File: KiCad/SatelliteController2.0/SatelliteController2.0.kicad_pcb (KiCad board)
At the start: 2 copper layers, 150 x 100 mm, 222 parts, among them J1 CONN_ICSP, J10 CONN_ISOLATED_RS485_REPEATER, J11 CONN_UMBILICAL, J12 CONN_ISOLATED_RS485_REPEATER, J13 CONN_ISOLATED_RS485, J14 RELAY_POWER, J15 IGNITOR, J16 CONN_SORENOID_VALVE, J2 CONN_USB, J3 USB_C_Receptacle_USB2.0_16P, J4 TO_CONVERTER, J5 FROM_CONVERTER, J6 DC_IN, J7 CONN_STATUS_PANEL, J8 CONN_PANEL_BOARD_2, J9 CONN_N2O_PRESS, Q1 TJ8S06M3L, Q10 AO3400A, Q11 AO3400A, Q12 AO3400A, Q13 AO3400A, Q2 2SC3325-Y, Q3 TJ8S06M3L, Q4 AO3400A, Q5 AO3400A, Q6 AO3400A, Q7 AO3400A, Q8 AO3400A, Q9 AO3400A, SW1 RUN_SW, SW2 KILL_SW, SW3 SAFETY_SW, SW4 RESET_SW, SW5 CHECK_SW, U1 ATMEGA2560-16AUR, U10 TLP785F, U11 TLP785F, U12 MCP3208, U2 FT232RNL, U3 USBLC6-2SC6, U4 TPS2116DRL, U5 NJM7805SDL1, U6 INA219BIDCNT, U7 INA219BIDCNT, U8 ADS1115IDGS, U9 ADM2587E, Y1 HUSG-16.000-20

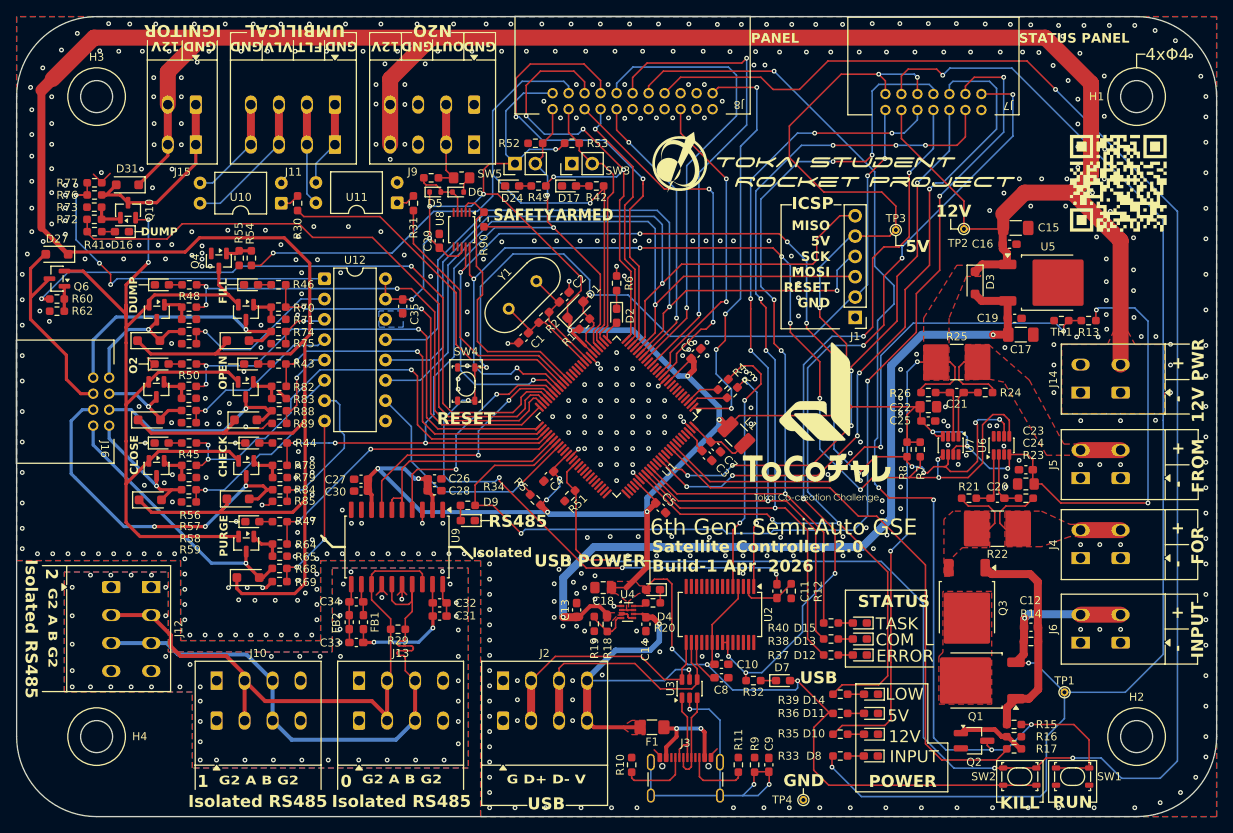
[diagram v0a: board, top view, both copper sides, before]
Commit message: シルクなどを調整
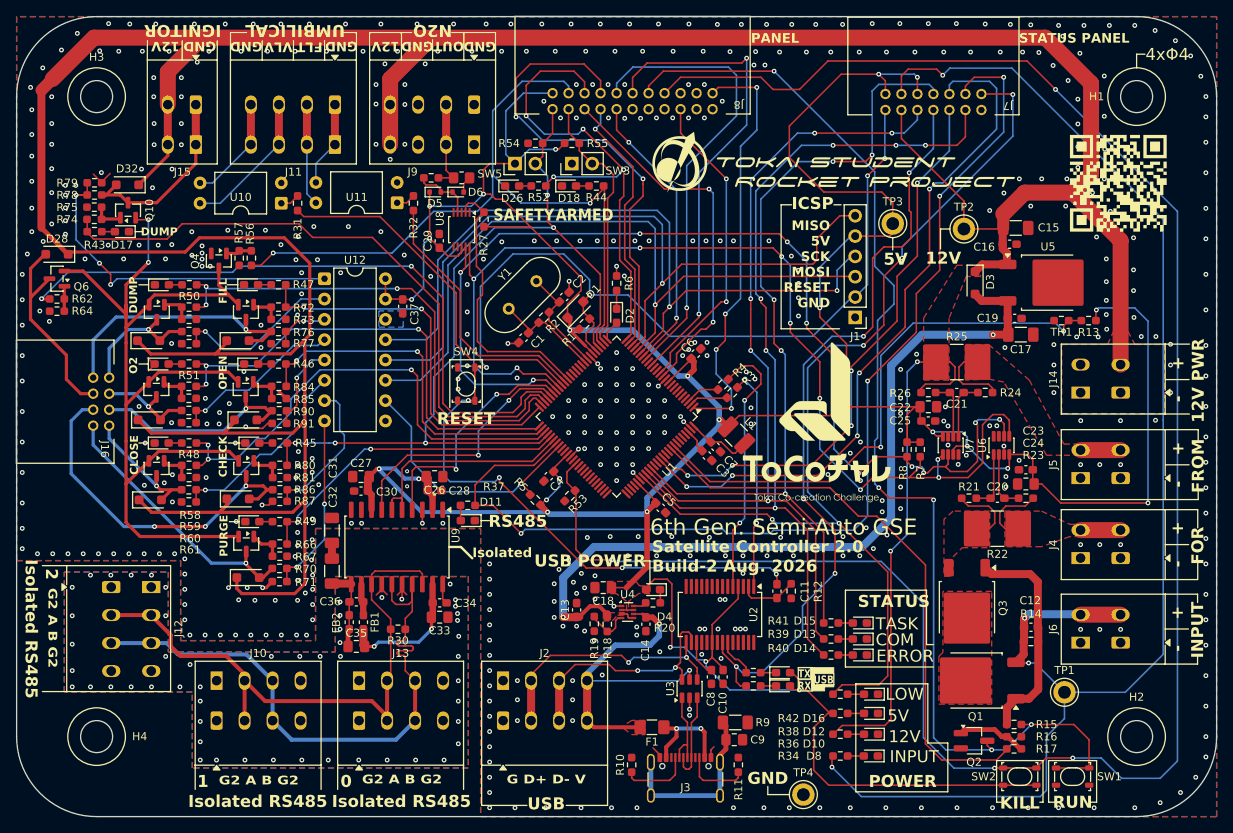
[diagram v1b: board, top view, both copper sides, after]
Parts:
- added C31: 470pF, Capacitor_SMD:C_1206_3216Metric_Pad1.33x1.80mm_HandSolder, F.Cu at (112.7, 119.4)
- added C32: 470pF, Capacitor_SMD:C_1206_3216Metric_Pad1.33x1.80mm_HandSolder, F.Cu at (112.7, 124.5)
- added D9: LED_O, LED_SMD:LED_0603_1608Metric_Pad1.05x0.95mm_HandSolder, F.Cu at (169.1, 137.2)
- added R35: 1kR, Resistor_SMD:R_0603_1608Metric_Pad0.98x0.95mm_HandSolder, F.Cu at (165.4, 137.2)
- C20, C21: value uF -> 0.1uF
- C26, C27: value 0.1uF -> 10uF; footprint Capacitor_SMD:C_0603_1608Metric_Pad1.08x0.95mm_HandSolder -> Capacitor_SMD:C_0805_2012Metric_Pad1.18x1.45mm_HandSolder
- C28, C30: value 0.01uF -> 0.1uF
- C33: renamed from C31; value 0.1uF -> 10uF; footprint Capacitor_SMD:C_0603_1608Metric_Pad1.08x0.95mm_HandSolder -> Capacitor_SMD:C_0805_2012Metric_Pad1.18x1.45mm_HandSolder
- C34: renamed from C32; value 0.01uF -> 0.1uF
- C35: renamed from C33; value 0.1uF -> 10uF; footprint Capacitor_SMD:C_0603_1608Metric_Pad1.08x0.95mm_HandSolder -> Capacitor_SMD:C_0805_2012Metric_Pad1.18x1.45mm_HandSolder
- C36: renamed from C34; value 0.01uF -> 0.1uF
- C9: value 4.7uF -> 10nF; footprint Capacitor_SMD:C_0603_1608Metric_Pad1.08x0.95mm_HandSolder -> Capacitor_SMD:C_0805_2012Metric_Pad1.18x1.45mm_HandSolder
- D2: value LED_G -> LED_O
- D7: value LED_B -> LED_G
- R18: value 348kR ±1% -> 348kR 1%
- R19: value 100kR ±1% -> 100kR 1%
- R21, R23, R24, R26: value 0R -> 10R
- R9: footprint Resistor_SMD:R_0603_1608Metric_Pad0.98x0.95mm_HandSolder -> Resistor_SMD:R_1206_3216Metric_Pad1.30x1.75mm_HandSolder
- TP1, TP2, TP3, TP4: footprint TestPoint:TestPoint_THTPad_D1.0mm_Drill0.5mm -> TestPoint:TestPoint_Keystone_5005-5009_Compact
- moved R9 5.82 mm to (163.1, 143.4), turned to 0 degrees
- moved C9 5.34 mm to (163.0, 145.5), turned to 180 degrees
- moved C10 1.60 mm to (161.6, 137.7), turned to 90 degrees
- moved C8 1.26 mm to (160.1, 137.7), turned to 90 degrees
- moved TP3 0.89 mm to (182.8, 81.0)
- moved TP4 0.67 mm to (171.6, 152.4)
- moved D7 0.66 mm to (169.1, 138.8)
- moved R33 0.66 mm to (165.4, 138.8)
- moved C35 0.50 mm to (115.7, 133.9)
- moved C27 0.33 mm to (116.3, 112.7)
- moved C26 0.29 mm to (125.5, 112.7)
- moved C33 0.14 mm to (126.1, 130.2)
- renumbered C35 to C37, D9 to D11, D11 to D12, D12 to D14, D14 to D16, D16 to D17, D17 to D18, D18 to D20, D20 to D22, D22 to D23, D23 to D24, D24 to D26, D26 to D27, D27 to D28, D28 to D29, D29 to D30, D30 to D31, D31 to D32, D32 to D33, D33 to D34, D34 to D35, R90 to R27, R27 to R28, R28 to R29, R29 to R30, R30 to R31, R31 to R32, R32 to R33, R33 to R34, R35 to R36, R34 to R37, R36 to R38, R38 to R39, R37 to R40, R40 to R41, R39 to R42, R41 to R43, R42 to R44, R44 to R45, R43 to R46, R46 to R47, R45 to R48, R47 to R49, R48 to R50, R50 to R51, R49 to R52, R51 to R53, R52 to R54, R53 to R55, R54 to R56, R55 to R57, R56 to R58, R57 to R59, R58 to R60, R59 to R61, R60 to R62, R61 to R63, R62 to R64, R63 to R65, R64 to R66, R65 to R67, R66 to R68, R67 to R69, R68 to R70, R69 to R71, R70 to R72, R71 to R73, R72 to R74, R73 to R75, R74 to R76, R75 to R77, R76 to R78, R77 to R79, R78 to R80, R79 to R81, R80 to R82, R81 to R83, R82 to R84, R83 to R85, R84 to R86, R85 to R87, R86 to R88, R87 to R89, R88 to R90, R89 to R91
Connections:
- U2 pad 23: CONN_LED_USB_ACCESS -> LED_USB_TXLED
- U3 pad 2: GNDPWR -> GND
- U3 pad 4: USB_D- -> USB_D+
- U3 pad 6: USB_D+ -> USB_D-
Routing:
- net GNDPWR: track 41.7 -> 22.4 mm, vias 3 -> 0
- net LED_USB_TXLED: track 0.00 -> 4.95 mm
- net CONN_LED_5V: track 497.8 -> 501.2 mm
- net CONN_LED_USB_ACCESS: track 94.3 -> 96.9 mm, vias 6 -> 5
- net Net-(C31-Pad2): track 0.00 -> 1.95 mm
- net Net-(D9-K): track 0.00 -> 1.92 mm
- net GND: track 32.9 -> 34.7 mm
- net GND2: track 20.1 -> 21.4 mm, vias 54 -> 53
- net Net-(U2-3V3OUT): track 5.62 -> 4.52 mm
- net USB_D-: track 31.1 -> 30.0 mm, vias 0 -> 2
- net USB_D+: track 31.2 -> 32.0 mm, vias 0 -> 2
- net /Periferal/Visoin: track 16.6 -> 17.2 mm
- net UART1_RX: track 29.6 -> 30.1 mm
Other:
- board text added: "RX"
- board text added: "Satellite Controller 2.0 Build-2 Aug. 2026"
- board text added: "TX"
- board text removed: "Satellite Controller 2.0 Build-1 Apr. 2026"

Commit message: BOM作成
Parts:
- added R31: RS485_A, Resistor_SMD:R_0805_2012Metric_Pad1.20x1.40mm_HandSolder, F.Cu at (119.5, 133.4)
- added R32: RS485_B, Resistor_SMD:R_0805_2012Metric_Pad1.20x1.40mm_HandSolder, F.Cu at (122.4, 133.4)
- D4: value LED_Y -> LED_O
- H1, H2, H3, H4: footprint MountingHole:MountingHole_4mm -> MountingHole:MountingHole_4.3mm_M4_Pad_Via
- R30: footprint Resistor_SMD:R_0603_1608Metric_Pad0.98x0.95mm_HandSolder -> Resistor_SMD:R_0805_2012Metric_Pad1.20x1.40mm_HandSolder
- moved R30 1.36 mm to (120.9, 130.4)
- moved G*** 0.66 mm to (211.6, 76.2)
- moved TP1 0.51 mm to (204.3, 139.1)
- moved R82 0.22 mm to (106.2, 111.0)
- moved R65 0.20 mm to (94.8, 101.2)
- moved R84 0.15 mm to (94.8, 91.3)
- renumbered R31 to R33, R32 to R34, R33 to R35, R34 to R36, R35 to R37, R36 to R38, R37 to R39, R38 to R40, R39 to R41, R40 to R42, R41 to R43, R42 to R44, R43 to R45, R44 to R46, R45 to R47, R46 to R48, R47 to R49, R48 to R50, R49 to R51, R50 to R52, R51 to R53, R52 to R54, R53 to R55, R54 to R56, R55 to R57, R56 to R58, R57 to R59, R58 to R60, R59 to R61, R60 to R62, R61 to R63, R62 to R64, R63 to R65, R64 to R66, R65 to R67, R66 to R68, R67 to R69, R68 to R70, R69 to R71, R70 to R72, R71 to R73, R72 to R74, R73 to R75, R74 to R76, R75 to R77, R76 to R78, R77 to R79, R78 to R80, R79 to R81, R80 to R82, R81 to R83, R82 to R84, R83 to R85, R84 to R86, R85 to R87, R86 to R88, R87 to R89, R88 to R90, R89 to R91, R90 to R92, R91 to R93
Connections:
- R30 pad 1: Net-(J10-Pin_3) -> Net-(U9-B)
- R30 pad 2: Net-(J10-Pin_2) -> Net-(U9-A)
- U9 pad 13: Net-(J10-Pin_2) -> Net-(U9-A)
- U9 pad 15: Net-(J10-Pin_3) -> Net-(U9-B)
- U9 pad 17: Net-(J10-Pin_3) -> Net-(U9-B)
- U9 pad 18: Net-(J10-Pin_2) -> Net-(U9-A)
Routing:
- net Net-(J10-Pin_3): track 77.0 -> 55.9 mm
- net Net-(J10-Pin_2): track 74.0 -> 55.4 mm
- net Net-(U9-A): track 0.00 -> 16.6 mm
- net Net-(U9-B): track 0.00 -> 13.9 mm
- net GND: track 34.7 -> 35.7 mm, vias 544 -> 586
- net CONN_LED_INPUT: track 181.7 -> 182.4 mm
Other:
- board text added: "A"
- board text added: "B"
